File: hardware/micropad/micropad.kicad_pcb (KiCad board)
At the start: 2 copper layers, 50.8 x 88.9 mm, 28 parts, among them J2 Conn_ARM_JTAG_SWD_10, J3 USB_B_Micro, SW1 SW_SPST, SW2 SW_SPST, SW3 SW_SPST, U1 LD1117S33TR_SOT223, U2 STM32F042K6Ux, U3 APA102

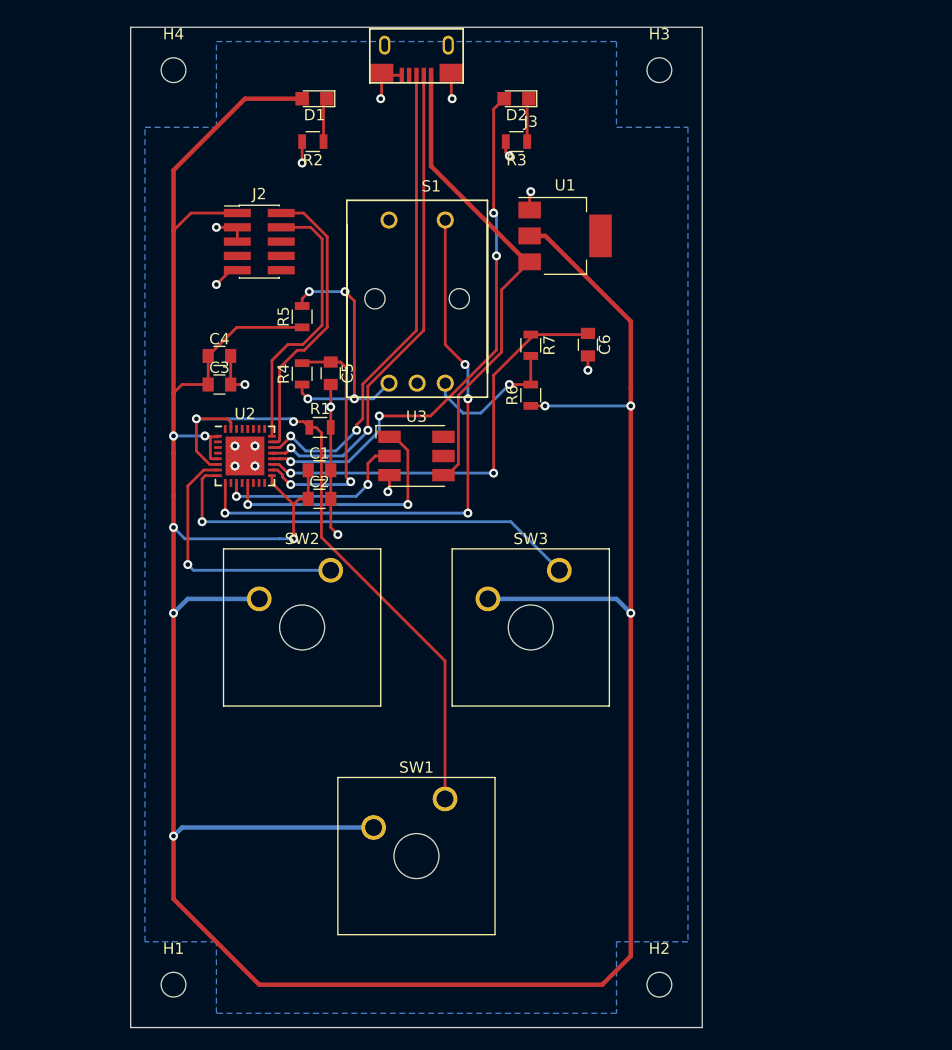
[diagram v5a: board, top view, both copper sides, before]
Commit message: Add fuse, fixup DRC and labels
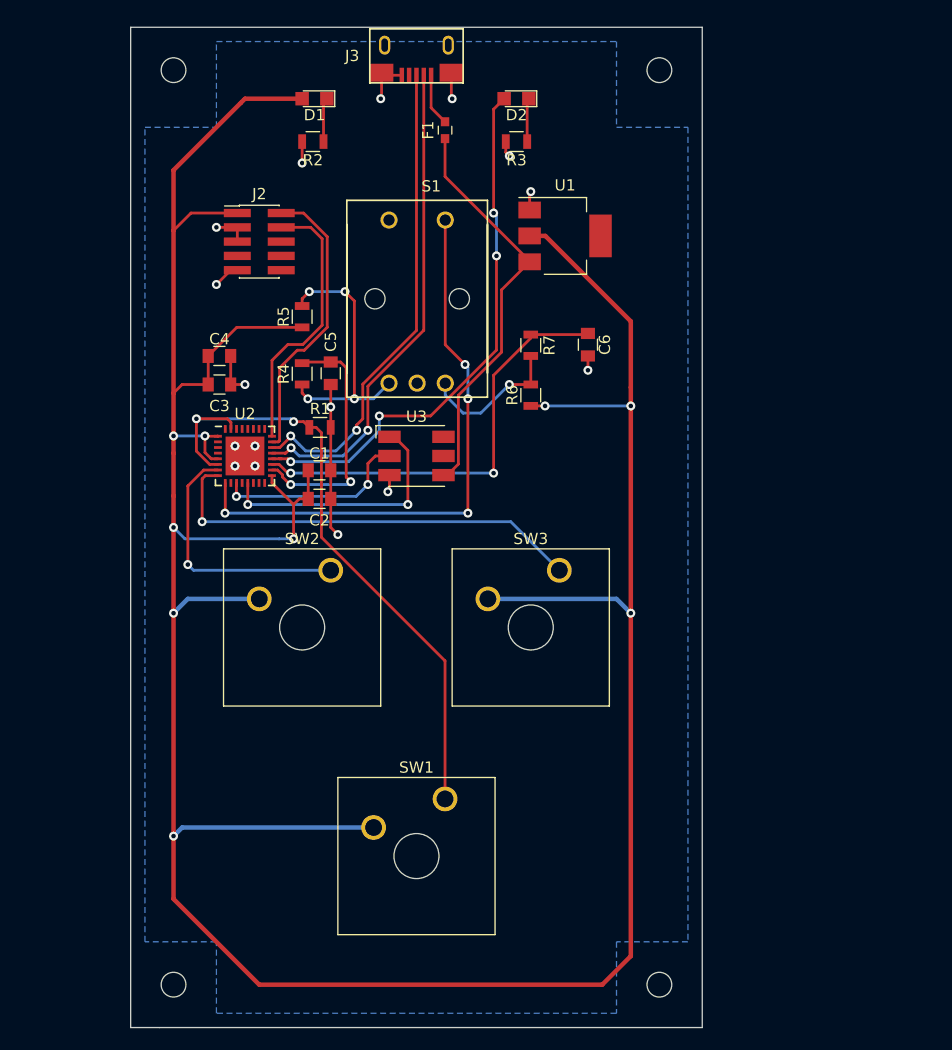
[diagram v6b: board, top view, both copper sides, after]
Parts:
- added F1: Fuse_Small, Capacitors_SMD:C_0603, F.Cu at (55.9, 21.8)
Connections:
- J3 pad 1: +5V -> Net-(F1-Pad2)
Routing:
- net +5V: track 42.7 -> 36.6 mm
- net Net-(F1-Pad2): track 0.00 -> 4.64 mm
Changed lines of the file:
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@@
     (thickness 1.6)
     (drawings 5)
-    (tracks 282)
+    (tracks 284)
     (zones 0)
-    (modules 28)
-    (nets 43)
+    (modules 29)
+    (nets 44)
   )
   (page A4)
@@
   (net 41 "Net-(U2-Pad3)")
   (net 42 "Net-(U2-Pad2)")
+  (net 43 "Net-(F1-Pad2)")
   (net_class Default "This is the default net class."
     (clearance 0.2)
@@
     (add_net "Net-(D1-Pad1)")
     (add_net "Net-(D2-Pad1)")
+    (add_net "Net-(F1-Pad2)")
     (add_net "Net-(J2-Pad10)")
     (add_net "Net-(J2-Pad6)")
@@
     (tags "capacitor 0805")
     (attr smd)
-    (fp_text reference C2 (at 0 -1.5) (layer F.SilkS)
+    (fp_text reference C2 (at 0 1.905) (layer F.SilkS)
       (effects (font (size 1 1) (thickness 0.15)))
     )
@@
     (tags "capacitor 0805")
     (attr smd)
-    (fp_text reference C3 (at 0 -1.5) (layer F.SilkS)
+    (fp_text reference C3 (at 0 1.905) (layer F.SilkS)
       (effects (font (size 1 1) (thickness 0.15)))
     )
@@
     (tags "capacitor 0805")
     (attr smd)
-    (fp_text reference C5 (at 0 -1.5 90) (layer F.SilkS)
+    (fp_text reference C5 (at -2.81 0 90) (layer F.SilkS)
       (effects (font (size 1 1) (thickness 0.15)))
     )
@@
   (module micropad:XKB-U254_USB (layer F.Cu)
     (at 53.34 15.24 180)
-    (fp_text reference J3 (at -10.16 -5.85) (layer F.SilkS)
-      (effects (font (size 1 1) (thickness 0.15)))
-    )
-    (fp_text value USB_B_Micro (at -10.16 -6.85) (layer F.Fab)
+    (fp_text reference J3 (at 5.715 0) (layer F.SilkS)
+      (effects (font (size 1 1) (thickness 0.15)))
+    )
+    (fp_text value USB_B_Micro (at 9.525 1.905) (layer F.Fab)
       (effects (font (size 1 1) (thickness 0.15)))
     )
@@
       (net 2 GND))
     (pad 1 smd rect (at -1.3 -1.725 180) (size 0.4 1.35) (layers F.Cu F.Paste F.Mask)
-      (net 14 +5V))
+      (net 43 "Net-(F1-Pad2)"))
     (pad 5 smd rect (at 1.3 -1.725 180) (size 0.4 1.35) (layers F.Cu F.Paste F.Mask)
       (net 2 GND))
@@
     (tags "mounting hole 2.2mm no annular m2")
     (attr virtual)
-    (fp_text reference H1 (at 0 -3.2) (layer F.SilkS)
+    (fp_text reference H1 (at 0 -3.2) (layer F.SilkS) hide
       (effects (font (size 1 1) (thickness 0.15)))
     )
@@
     (tags "mounting hole 2.2mm no annular m2")
     (attr virtual)
-    (fp_text reference H2 (at 0 -3.2) (layer F.SilkS)
+    (fp_text reference H2 (at 0 -3.2) (layer F.SilkS) hide
       (effects (font (size 1 1) (thickness 0.15)))
     )
@@
     (tags "mounting hole 2.2mm no annular m2")
     (attr virtual)
-    (fp_text reference H3 (at 0 -3.2) (layer F.SilkS)
+    (fp_text reference H3 (at -3.81 0) (layer F.SilkS) hide
       (effects (font (size 1 1) (thickness 0.15)))
     )
@@
     (tags "mounting hole 2.2mm no annular m2")
     (attr virtual)
-    (fp_text reference H4 (at 0 -3.2) (layer F.SilkS)
+    (fp_text reference H4 (at 3.81 0) (layer F.SilkS) hide
       (effects (font (size 1 1) (thickness 0.15)))
     )
@@
     )
   )
+  (module Capacitors_SMD:C_0603 (layer F.Cu)
+    (at 55.88 21.844 90)
+    (descr "Capacitor SMD 0603, reflow soldering, AVX (see smccp.pdf)")
+    (tags "capacitor 0603")
+    (attr smd)
+    (fp_text reference F1 (at 0 -1.5 90) (layer F.SilkS)
+      (effects (font (size 1 1) (thickness 0.15)))
+    )
+    (fp_text value Fuse_Small (at 0 1.5 90) (layer F.Fab)
+      (effects (font (size 1 1) (thickness 0.15)))
+    )
+    (fp_text user %R (at 0 0 90) (layer F.Fab)
+      (effects (font (size 0.3 0.3) (thickness 0.075)))
+    )
+    (fp_line (start 1.4 0.65) (end -1.4 0.65) (layer F.CrtYd) (width 0.05))
+    (fp_line (start 1.4 0.65) (end 1.4 -0.65) (layer F.CrtYd) (width 0.05))
+    (fp_line (start -1.4 -0.65) (end -1.4 0.65) (layer F.CrtYd) (width 0.05))
+    (fp_line (start -1.4 -0.65) (end 1.4 -0.65) (layer F.CrtYd) (width 0.05))
+    (fp_line (start 0.35 0.6) (end -0.35 0.6) (layer F.SilkS) (width 0.12))
+    (fp_line (start -0.35 -0.6) (end 0.35 -0.6) (layer F.SilkS) (width 0.12))
+    (fp_line (start -0.8 -0.4) (end 0.8 -0.4) (layer F.Fab) (width 0.1))
+    (fp_line (start 0.8 -0.4) (end 0.8 0.4) (layer F.Fab) (width 0.1))
+    (fp_line (start 0.8 0.4) (end -0.8 0.4) (layer F.Fab) (width 0.1))
+    (fp_line (start -0.8 0.4) (end -0.8 -0.4) (layer F.Fab) (width 0.1))
+    (pad 1 smd rect (at -0.75 0 90) (size 0.8 0.75) (layers F.Cu F.Paste F.Mask)
+      (net 14 +5V))
+    (pad 2 smd rect (at 0.75 0 90) (size 0.8 0.75) (layers F.Cu F.Paste F.Mask)
+      (net 43 "Net-(F1-Pad2)"))
+    (model Capacitors_SMD.3dshapes/C_0603.wrl
+      (at (xyz 0 0 0))
+      (scale (xyz 1 1 1))
+      (rotate (xyz 0 0 0))
+    )
+  )
   (gr_line (start 30.48 101.6) (end 78.74 101.6) (layer Edge.Cuts) (width 0.05))
   (gr_line (start 27.94 101.6) (end 30.48 101.6) (layer Edge.Cuts) (width 0.05))
@@
   (segment (start 42.418 58.166) (end 41.148 58.166) (width 0.25) (layer B.Cu) (net 1))
   (segment (start 35.1 51.05) (end 35.024999 50.974999) (width 0.25) (layer F.Cu) (net 1))
-  (segment (start 35.024999 50.974999) (end 35.024999 49.164999) (width 0.25) (layer F.Cu) (net 1))
   (segment (start 35.7 51.05) (end 35.1 51.05) (width 0.25) (layer F.Cu) (net 1))
-  (segment (start 35.024999 49.164999) (end 35.089999 49.099999) (width 0.25) (layer F.Cu) (net 1))
-  (segment (start 35.650001 49.099999) (end 35.7 49.05) (width 0.25) (layer F.Cu) (net 1))
-  (segment (start 35.089999 49.099999) (end 35.650001 49.099999) (width 0.25) (layer F.Cu) (net 1))
-  (via (at 34.544 49.022) (size 0.8) (drill 0.4) (layers F.Cu B.Cu) (net 1))
-  (segment (start 34.621999 49.099999) (end 34.544 49.022) (width 0.25) (layer F.Cu) (net 1))
-  (segment (start 35.089999 49.099999) (end 34.621999 49.099999) (width 0.25) (layer F.Cu) (net 1))
-  (via (at 31.75 49.022) (size 0.8) (drill 0.4) (layers F.Cu B.Cu) (net 1))
-  (segment (start 34.544 49.022) (end 31.75 49.022) (width 0.25) (layer B.Cu) (net 1))
   (via (at 64.77 46.355) (size 0.8) (drill 0.4) (layers F.Cu B.Cu) (net 1))
   (segment (start 64.765 46.35) (end 64.77 46.355) (width 0.25) (layer F.Cu) (net 1))
@@
   (via (at 72.39 46.355) (size 0.8) (drill 0.4) (layers F.Cu B.Cu) (net 1))
   (segment (start 64.77 46.355) (end 72.39 46.355) (width 0.25) (layer B.Cu) (net 1))
+  (via (at 34.544 49.022) (size 0.8) (drill 0.4) (layers F.Cu B.Cu) (net 1))
+  (segment (start 34.544 49.022) (end 31.75 49.022) (width 0.25) (layer B.Cu) (net 1))
+  (via (at 31.75 49.022) (size 0.8) (drill 0.4) (layers F.Cu B.Cu) (net 1))
+  (segment (start 34.621999 49.099999) (end 34.544 49.022) (width 0.25) (layer F.Cu) (net 1))
+  (segment (start 34.5709 49.0489) (end 34.544 49.022) (width 0.25) (layer F.Cu) (net 1))
+  (segment (start 35.6989 49.0489) (end 34.5709 49.0489) (width 0.25) (layer F.Cu) (net 1))
+  (segment (start 34.544 50.494) (end 34.544 49.022) (width 0.25) (layer F.Cu) (net 1))
+  (segment (start 35.1 51.05) (end 34.544 50.494) (width 0.25) (layer F.Cu) (net 1))
   (via (at 38.1 44.45) (size 0.8) (drill 0.4) (layers F.Cu B.Cu) (net 2))
   (segment (start 36.83 44.45) (end 38.1 44.45) (width 0.25) (layer F.Cu) (net 2))
@@
   (segment (start 42.742998 41.402) (end 41.175001 42.969997) (width 0.25) (layer F.Cu) (net 13))
   (segment (start 43.369412 41.402) (end 42.742998 41.402) (width 0.25) (layer F.Cu) (net 13))
-  (segment (start 54.64 25.034) (end 54.64 16.965) (width 0.4) (layer F.Cu) (net 14))
-  (segment (start 63.148 33.542) (end 54.64 25.034) (width 0.4) (layer F.Cu) (net 14))
   (segment (start 63.398 33.542) (end 63.148 33.542) (width 0.4) (layer F.Cu) (net 14))
   (segment (start 57.065001 45.410171) (end 57.065001 51.519999) (width 0.25) (layer F.Cu) (net 14))
@@
   (segment (start 56.085 52.5) (end 55.74 52.5) (width 0.25) (layer F.Cu) (net 14))
   (segment (start 57.065001 51.519999) (end 56.085 52.5) (width 0.25) (layer F.Cu) (net 14))
+  (segment (start 63.398 33.483002) (end 63.398 33.542) (width 0.25) (layer F.Cu) (net 14))
+  (segment (start 55.88 25.965002) (end 63.398 33.483002) (width 0.25) (layer F.Cu) (net 14))
+  (segment (start 55.88 22.594) (end 55.88 25.965002) (width 0.25) (layer F.Cu) (net 14))
   (segment (start 53.99 16.965) (end 53.99 39.631238) (width 0.25) (layer F.Cu) (net 15))
   (segment (start 53.99 39.631238) (end 49.022 44.599238) (width 0.25) (layer F.Cu) (net 15))
@@
   (segment (start 37.338 53.212) (end 37.35 53.2) (width 0.25) (layer F.Cu) (net 25))
   (segment (start 37.338 54.393) (end 37.338 53.212) (width 0.25) (layer F.Cu) (net 25))
+  (segment (start 54.64 19.854) (end 54.64 16.965) (width 0.25) (layer F.Cu) (net 43))
+  (segment (start 55.88 21.094) (end 54.64 19.854) (width 0.25) (layer F.Cu) (net 43))
   (zone (net 2) (net_name GND) (layer B.Cu) (hatch edge 0.508)
     (connect_pads (clearance 0.508))

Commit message: Reduce board width
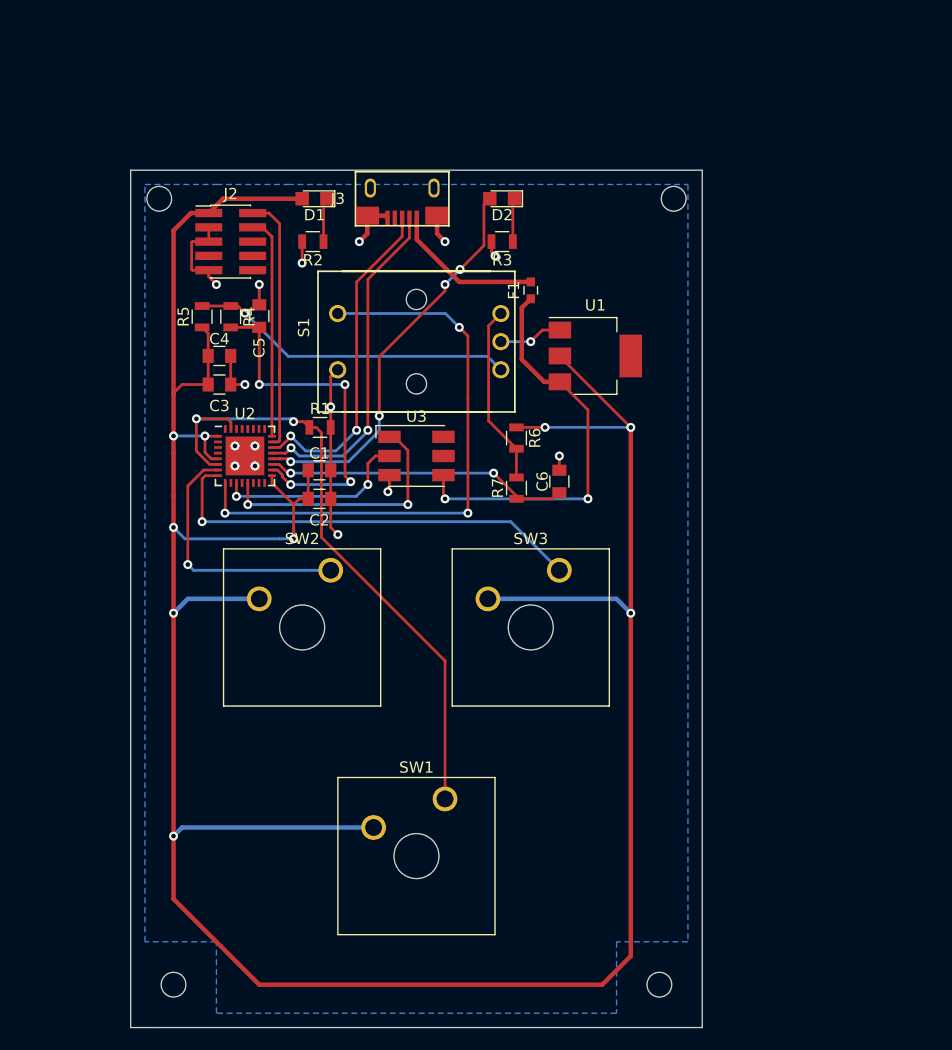
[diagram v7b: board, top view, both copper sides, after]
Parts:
- moved F1 16.1 mm to (63.5, 36.1)
- moved J3 12.8 mm to (52.1, 27.9)
- moved R7 12.8 mm to (62.2, 53.7), turned to 90 degrees
- moved C6 12.4 mm to (66.0, 53.1), turned to 90 degrees
- moved H3 11.5 mm to (76.2, 27.9)
- moved H4 11.5 mm to (30.5, 27.9)
- moved U1 11.0 mm to (69.2, 41.9)
- moved D2 8.98 mm to (61.0, 27.9)
- moved R3 8.98 mm to (61.0, 31.8)
- moved D1 8.89 mm to (44.3, 27.9)
- moved R2 8.89 mm to (44.1, 31.8)
- moved R5 8.89 mm to (34.3, 38.4)
- moved C5 8.13 mm to (39.4, 38.4), turned to 90 degrees
- moved R4 8.13 mm to (36.8, 38.4), turned to 270 degrees
- moved R6 4.02 mm to (62.2, 49.2), turned to 270 degrees
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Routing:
- net +3V3: track 290.9 -> 259.8 mm
- net /USB_DM: track 43.6 -> 30.4 mm
- net /USB_DP: track 43.0 -> 29.8 mm
- net /LED_USR: track 48.0 -> 35.7 mm
- net /ENC_B: track 38.8 -> 27.2 mm
- net GND: track 37.3 -> 48.0 mm
- net /ENC_A: track 22.2 -> 31.8 mm, vias 2 -> 4
- net Net-(F1-Pad2): track 4.64 -> 13.6 mm
- net Net-(R4-Pad1): track 23.9 -> 28.9 mm, vias 4 -> 1
- net /SWCLK: track 24.2 -> 19.8 mm
- net Net-(R6-Pad2): track 12.9 -> 16.0 mm, vias 1 -> 0
- net /SWDIO: track 25.9 -> 23.7 mm
- net /ENC_BTN: track 51.2 -> 52.4 mm, vias 4 -> 3
- net +5V: vias 0 -> 2
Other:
- board size 50.8 x 88.9 mm -> 50.8 x 76.2 mm

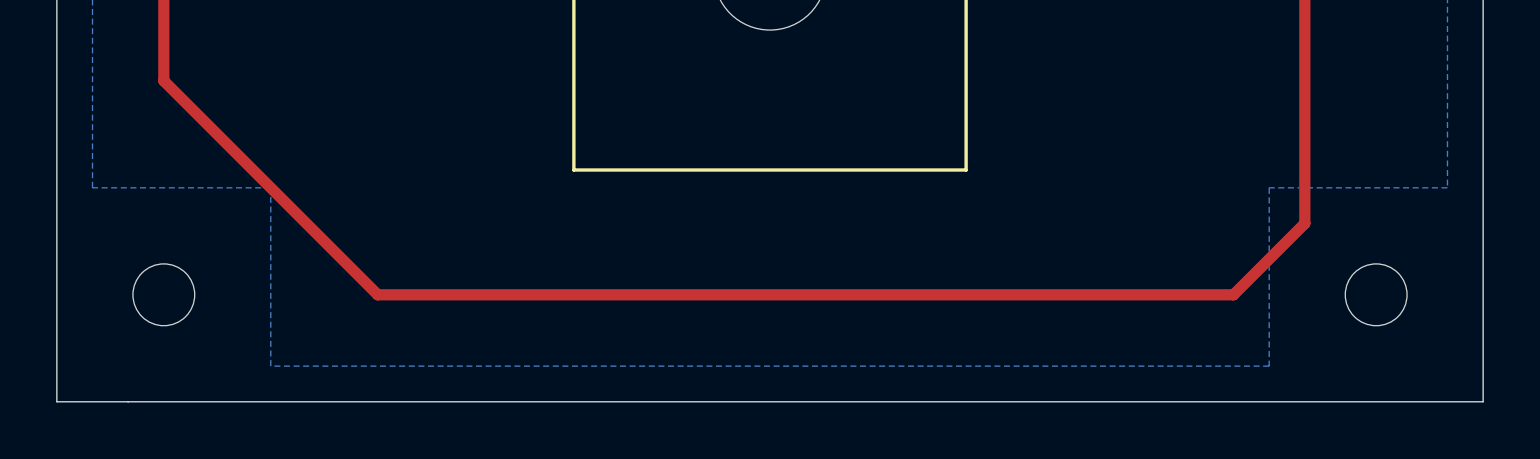
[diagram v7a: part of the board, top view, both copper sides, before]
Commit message: Line up mounting holes
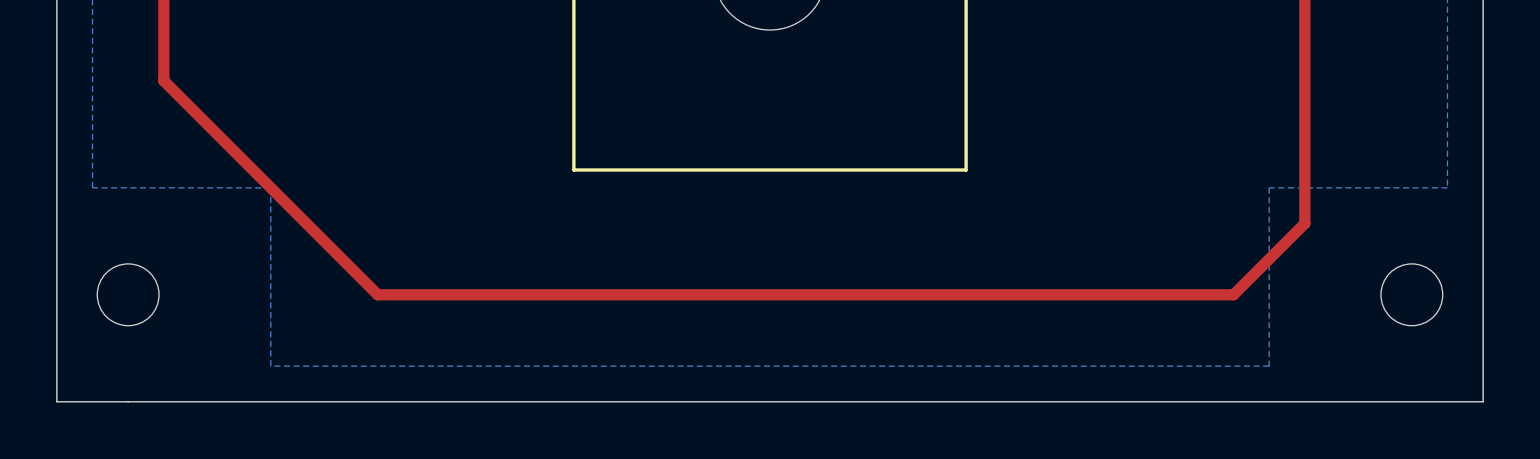
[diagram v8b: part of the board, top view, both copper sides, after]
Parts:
- moved H1 1.27 mm to (30.5, 97.8)
- moved H2 1.27 mm to (76.2, 97.8)
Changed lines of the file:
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@@
   )
   (module Mounting_Holes:MountingHole_2.2mm_M2 (layer F.Cu)
-    (at 31.75 97.79)
+    (at 30.48 97.79)
     (descr "Mounting Hole 2.2mm, no annular, M2")
     (tags "mounting hole 2.2mm no annular m2")
@@
   )
   (module Mounting_Holes:MountingHole_2.2mm_M2 (layer F.Cu)
-    (at 74.93 97.79)
+    (at 76.2 97.79)
     (descr "Mounting Hole 2.2mm, no annular, M2")
     (tags "mounting hole 2.2mm no annular m2")
